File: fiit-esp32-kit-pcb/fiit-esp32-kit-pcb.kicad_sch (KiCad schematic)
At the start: 38 parts, among them J1 Conn_01x22_Pin, J2 Conn_01x22_Pin, J5 Conn_ARM_JTAG_SWD_10, J6 Conn_01x06_Pin, J7 QWIIC - I2C, SW5 SPST NO, U1 ESP32-S3-WROOM-1, U2 SY8089AAAC

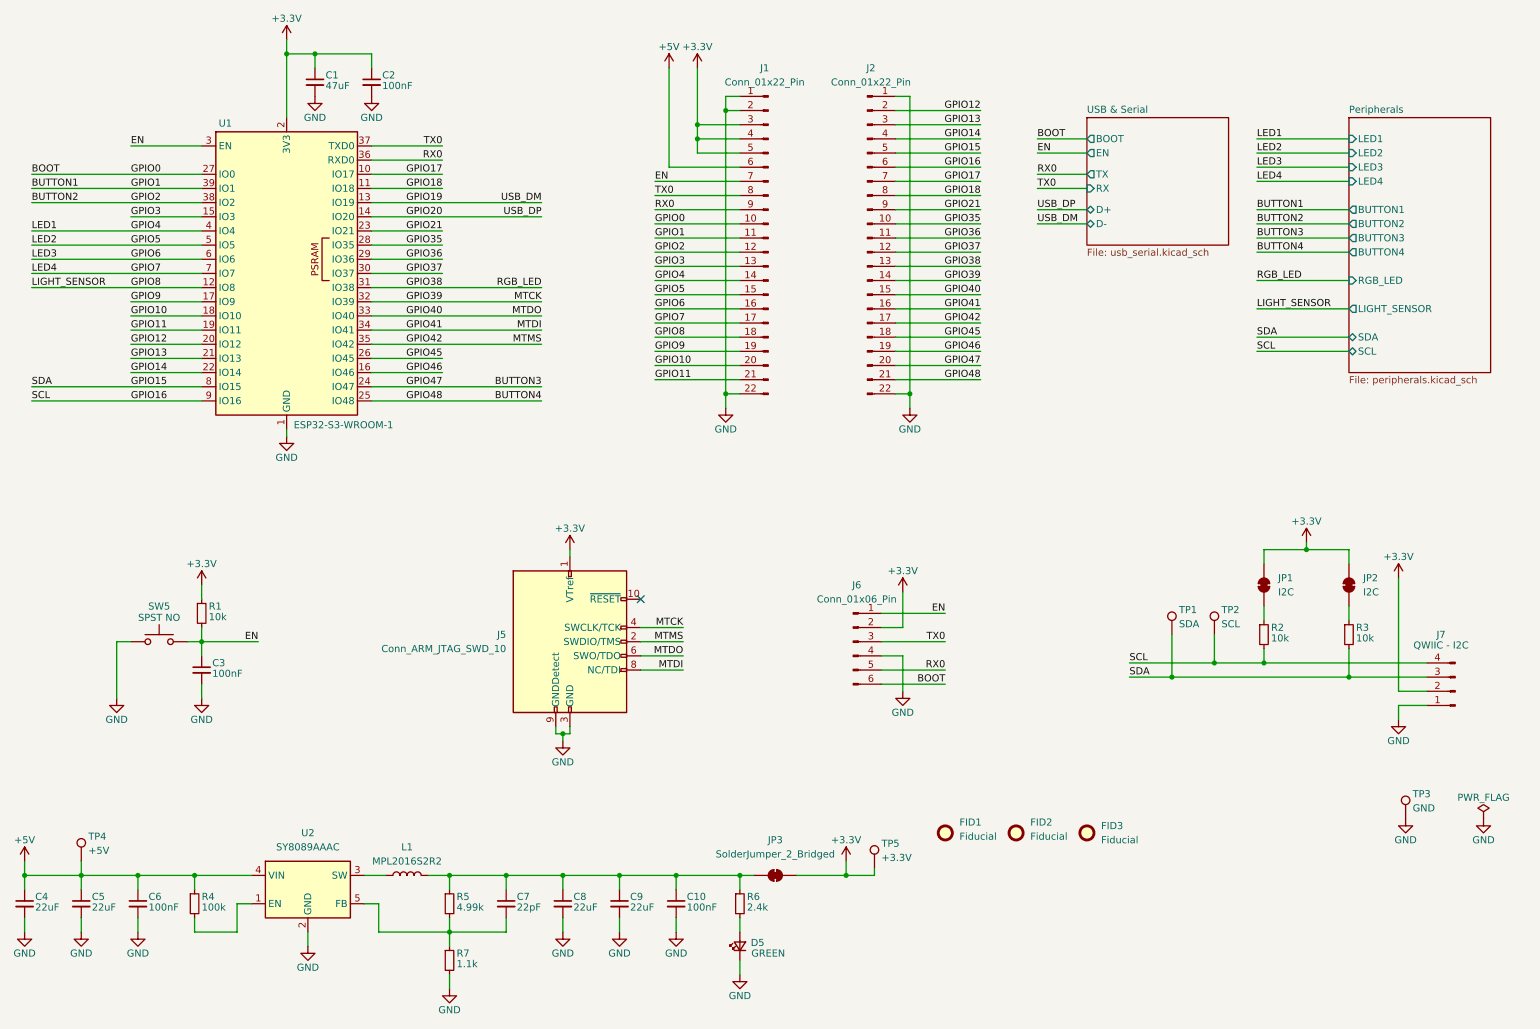
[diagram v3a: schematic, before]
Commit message: updated components placement (unrouted 237)
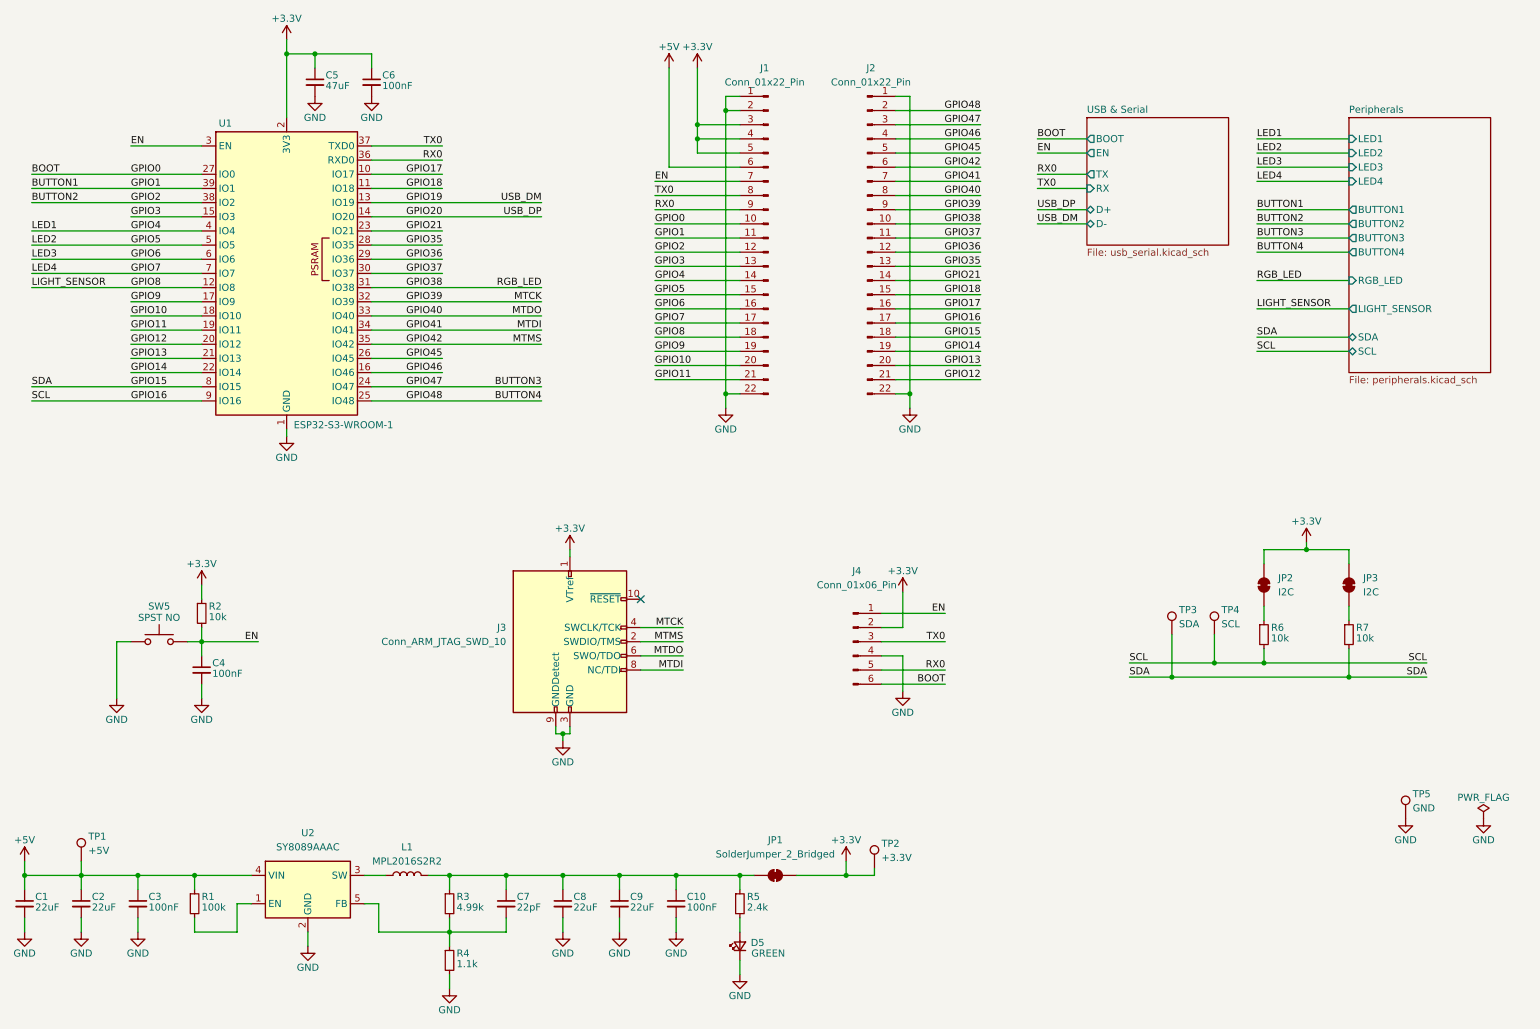
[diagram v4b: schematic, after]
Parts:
- removed FID1, FID2, FID3: Fiducial, Fiducial:Fiducial_0.5mm_Mask1mm, symbol Mechanical:Fiducial
- removed J7: QWIIC - I2C, Connector_JST:JST_SH_SM04B-SRSS-TB_1x04-1MP_P1.00mm_Horizontal, symbol Connector:Conn_01x04_Pin
- J3: renamed from J5; footprint Connector_IDC:IDC-Header_2x05_P2.54mm_Vertical -> Connector_PinHeader_1.27mm:PinHeader_2x05_P1.27mm_Vertical_SMD
- J4: renamed from J6; footprint Connector_IDC:IDC-Header_2x03_P2.54mm_Vertical -> Connector_PinHeader_1.27mm:PinHeader_2x03_P1.27mm_Vertical_SMD
- renumbered C4 to C1, C5 to C2, C6 to C3, C3 to C4, C1 to C5, C2 to C6, JP3 to JP1, JP1 to JP2, JP2 to JP3, R4 to R1, R1 to R2, R5 to R3, R7 to R4, R6 to R5, R2 to R6, R3 to R7, TP4 to TP1, TP5 to TP2, TP1 to TP3, TP2 to TP4, TP3 to TP5
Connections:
- net BUTTON3: now also J2.3 (Pin_3); no longer J2.20 (Pin_20)
- net BUTTON4: now also J2.2 (Pin_2); no longer J2.21 (Pin_21)
- net GPIO12: now also J2.21 (Pin_21); no longer J2.2 (Pin_2)
- net GPIO13: now also J2.20 (Pin_20); no longer J2.3 (Pin_3)
- net GPIO14: now also J2.19 (Pin_19); no longer J2.4 (Pin_4)
- net GPIO15: now also J2.18 (Pin_18); no longer J2.5 (Pin_5)
- net GPIO16: now also J2.17 (Pin_17); no longer J2.6 (Pin_6)
- net GPIO17: now also J2.16 (Pin_16); no longer J2.7 (Pin_7)
- net GPIO18: now also J2.15 (Pin_15); no longer J2.8 (Pin_8)
- net GPIO21: now also J2.14 (Pin_14); no longer J2.9 (Pin_9)
- net GPIO35: now also J2.13 (Pin_13); no longer J2.10 (Pin_10)
- net GPIO36: now also J2.12 (Pin_12); no longer J2.11 (Pin_11)
- net GPIO37: now also J2.11 (Pin_11); no longer J2.12 (Pin_12)
- net GPIO38: now also J2.10 (Pin_10); no longer J2.13 (Pin_13)
- net GPIO39: now also J2.9 (Pin_9); no longer J2.14 (Pin_14)
- net GPIO40: now also J2.8 (Pin_8); no longer J2.15 (Pin_15)
- net GPIO41: now also J2.7 (Pin_7); no longer J2.16 (Pin_16)
- net GPIO42: now also J2.6 (Pin_6); no longer J2.17 (Pin_17)
- net GPIO45: now also J2.5 (Pin_5); no longer J2.18 (Pin_18)
- net GPIO46: now also J2.4 (Pin_4); no longer J2.19 (Pin_19)

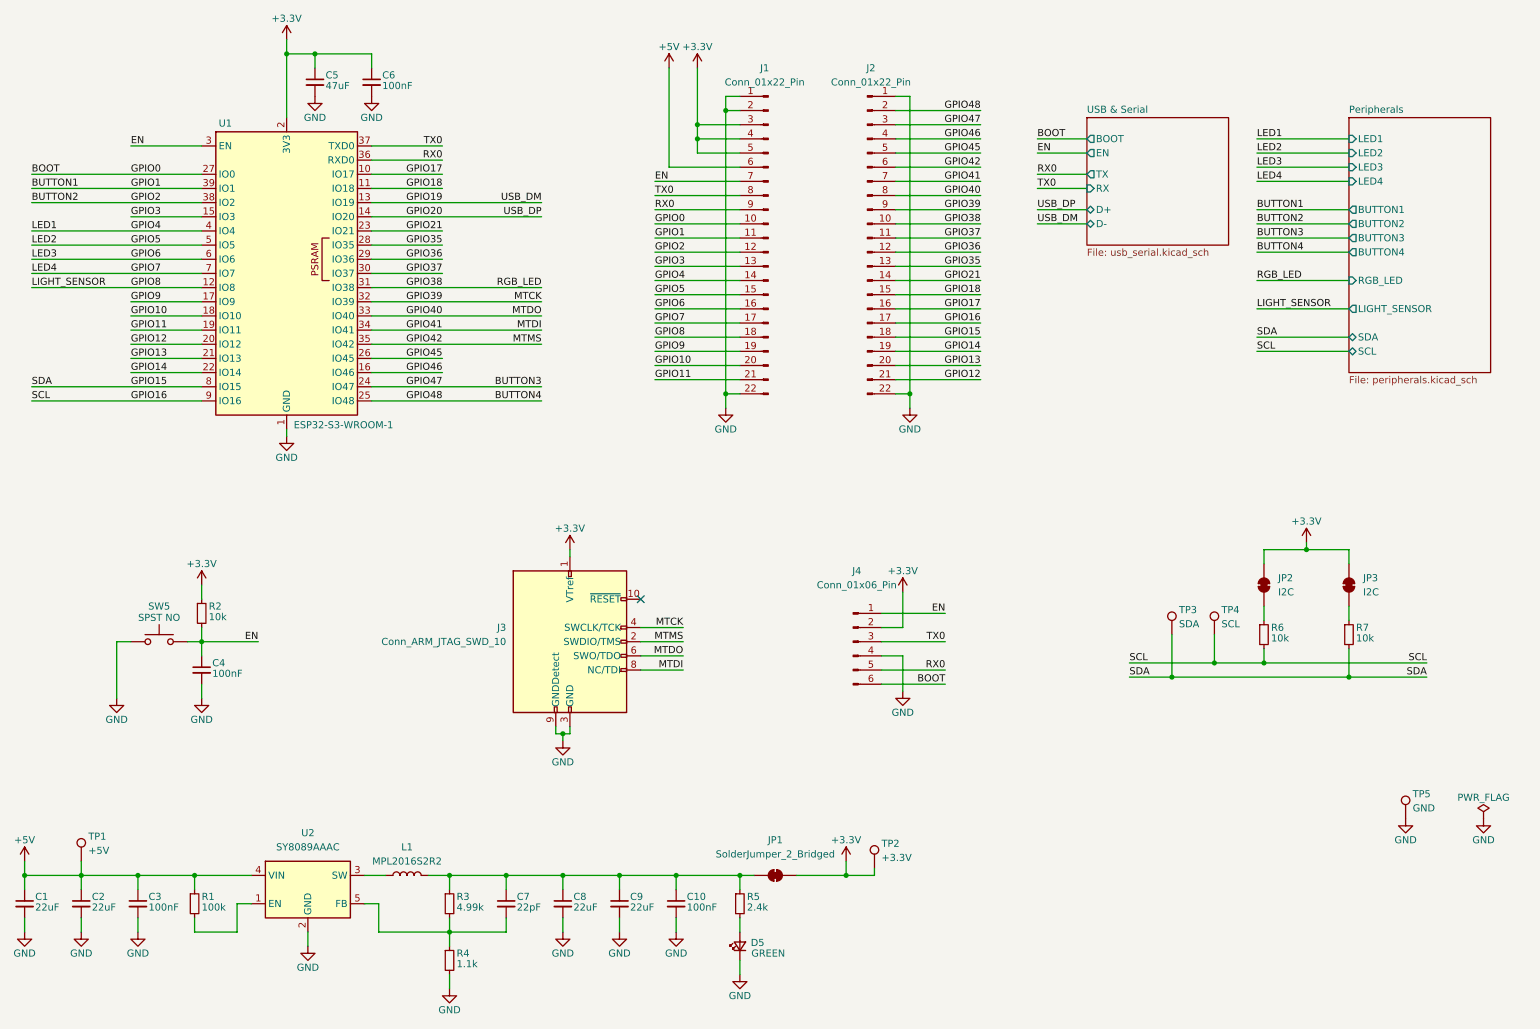
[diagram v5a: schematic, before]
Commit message: added some tracks (unrouted 0 !!!)
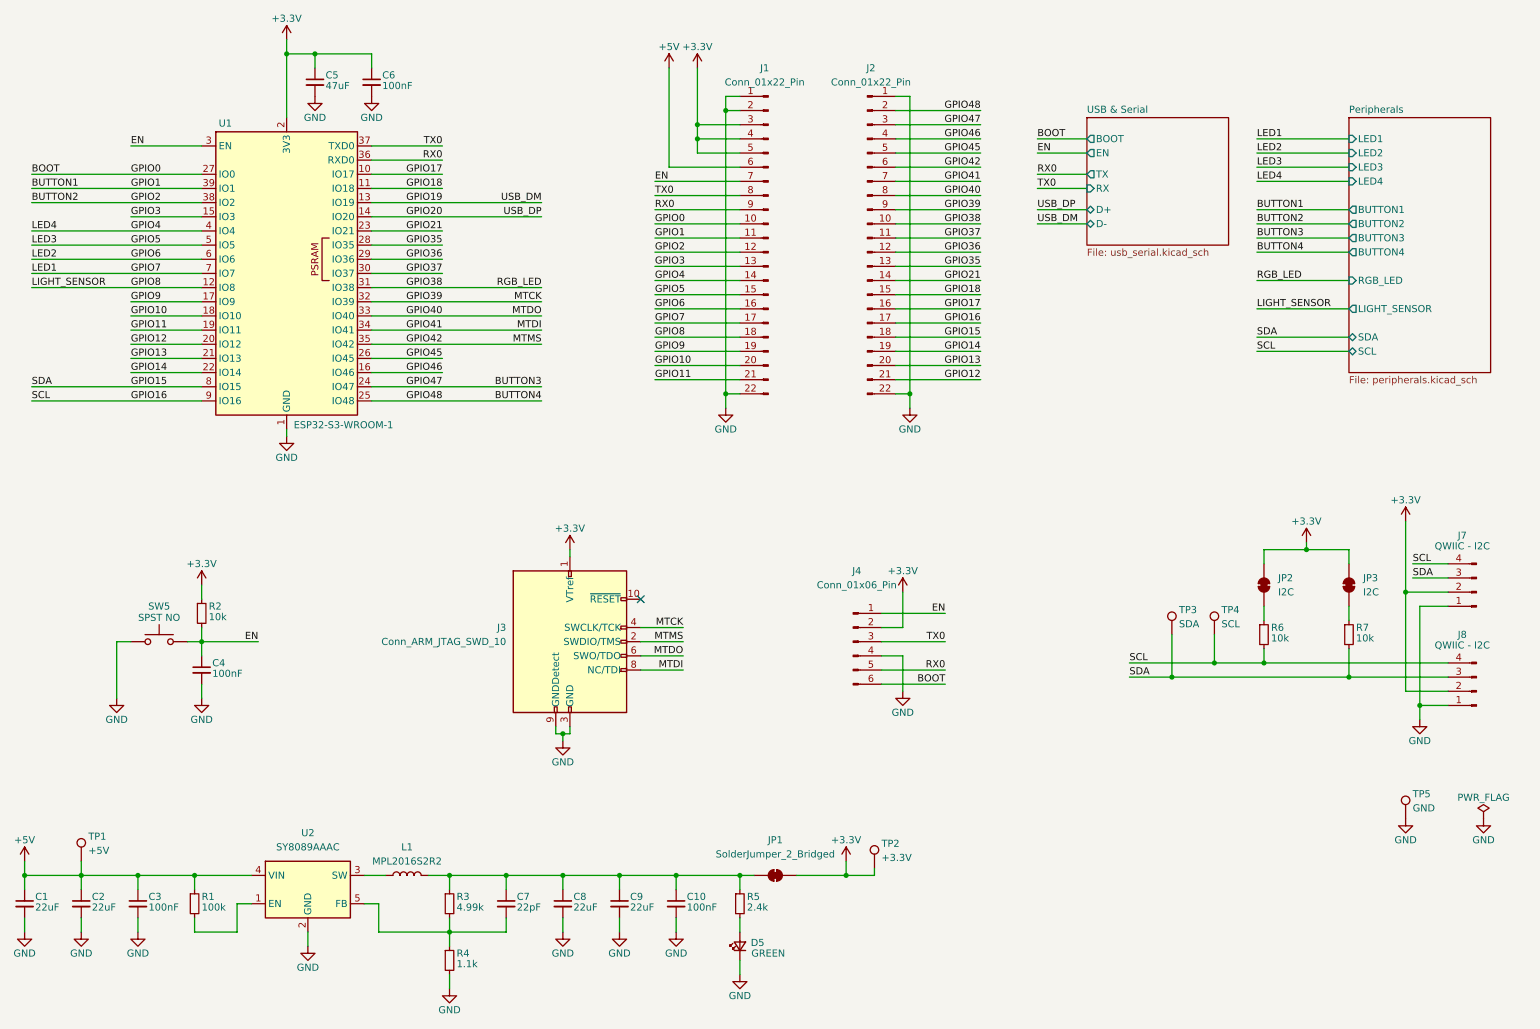
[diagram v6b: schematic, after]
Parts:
- added J7, J8: QWIIC - I2C, Connector_JST:JST_SH_SM04B-SRSS-TB_1x04-1MP_P1.00mm_Horizontal, symbol Connector:Conn_01x04_Pin
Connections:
- net +3.3V: now also J7.2 (Pin_2), J8.2 (Pin_2)
- net GND: now also J7.1 (Pin_1), J8.1 (Pin_1)
- net GPIO15: now also J7.3 (Pin_3), J8.3 (Pin_3)
- net GPIO16: now also J7.4 (Pin_4), J8.4 (Pin_4)
